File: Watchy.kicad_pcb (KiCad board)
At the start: 2 copper layers, 33.8 x 46 mm, 70 parts, among them J1 FPC24(0.5MM), J2 Micro USB, J3 Battery, M1 Vibration_Motor, Q1 AO3400A, Q2 UMH3N, Q4 CJ2301, Q5 S8050, SW1 BTN, SW2 BTN, SW3 BTN, SW4 BTN, U1 ESP32-PICO-D4, U2 ME6211C33M5G-N, U3 CP2102, U4 BMA423, U5 TP4054, U6 PCF8563BS, Y1 32.768KHz

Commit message: update to kicad 7
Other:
- net class Default removed

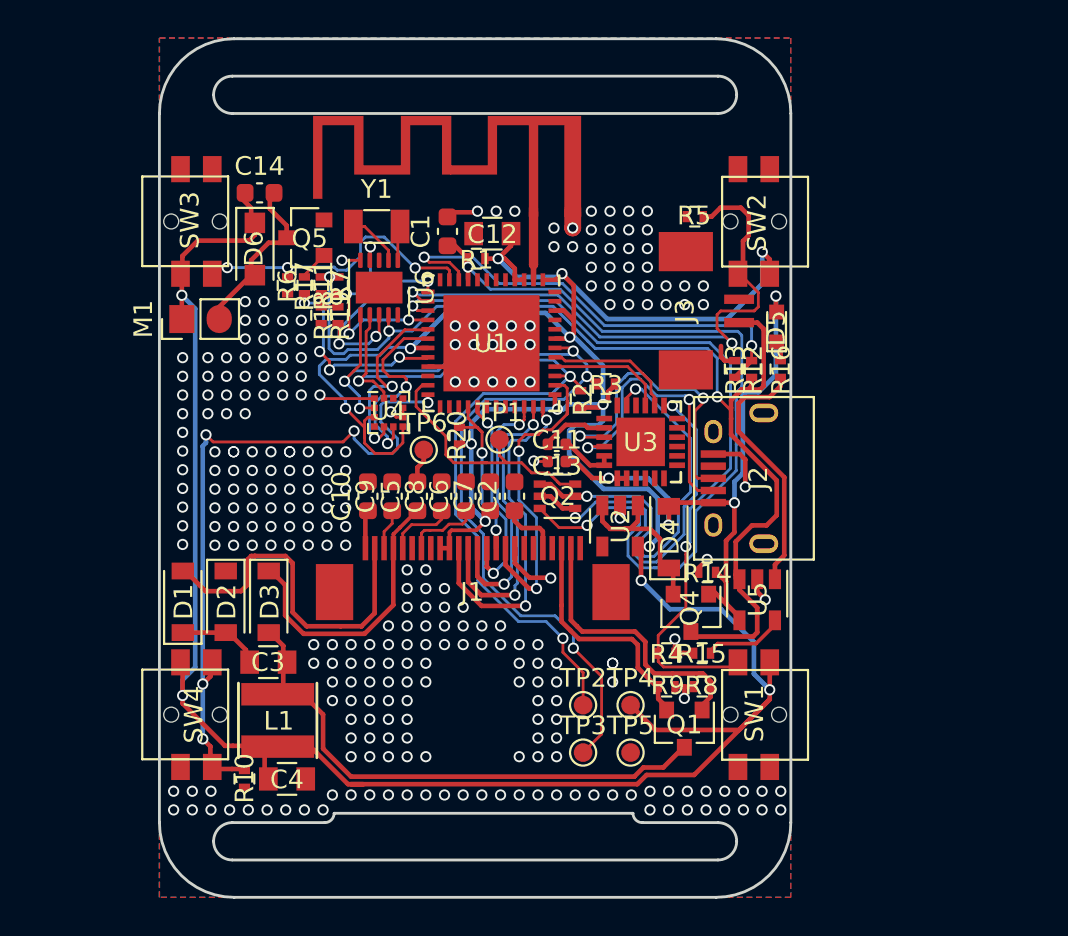
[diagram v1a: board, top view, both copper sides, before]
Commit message: add vib_mot footprint, remove all traces, rough positions
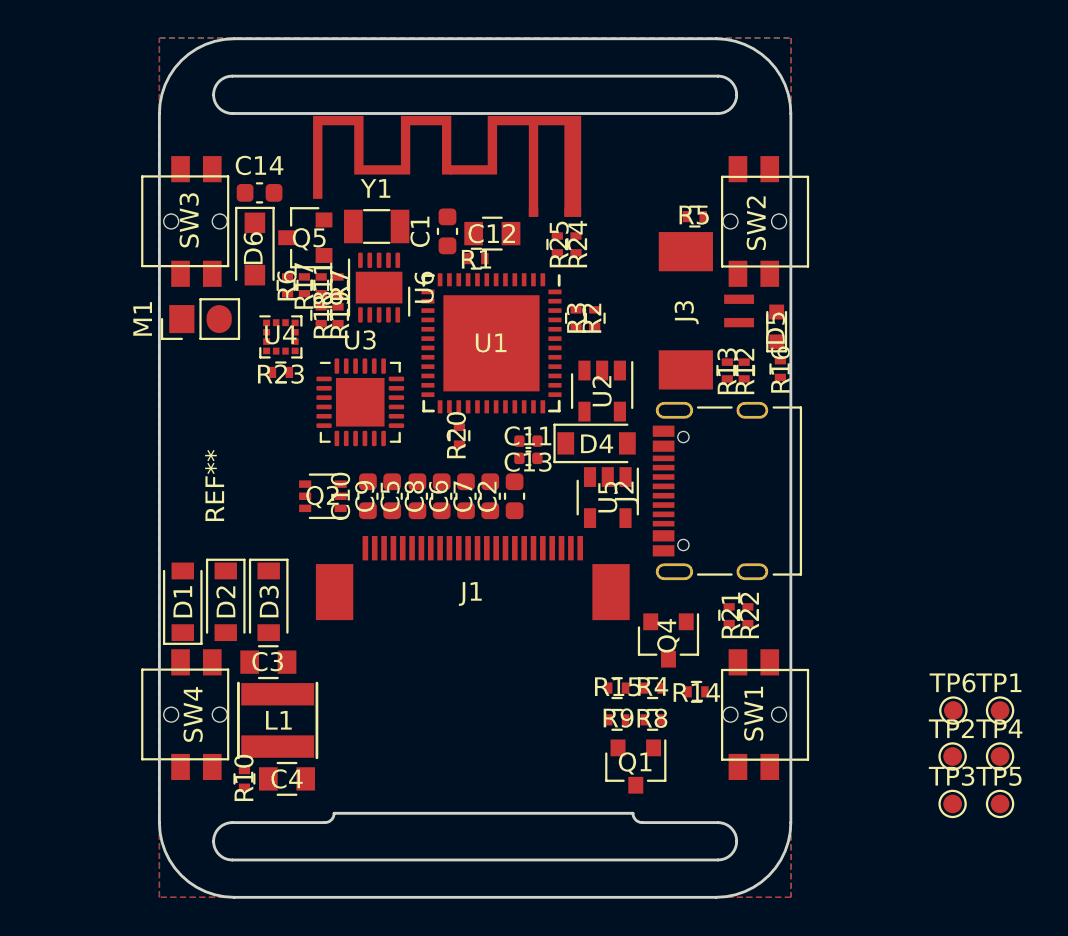
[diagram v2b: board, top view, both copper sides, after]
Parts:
- removed G***: LOGO, Watchy:sqfmi_duck
- removed G***: LOGO, Watchy:sqfmi_logo
- removed the REF** at (85.6, 93.2)
- added R21: 5.1k, Watchy:R_0402, F.Cu at (99.2, 101.0)
- added R22: 5.1k, Watchy:R_0402, F.Cu at (100.2, 101.0)
- added R23: 10K, Watchy:R_0402, F.Cu at (75.2, 88.0)
- added R24: 15k, Watchy:R_0402, F.Cu at (91.0, 81.2)
- added R25: 22k, Watchy:R_0402, F.Cu at (90.0, 81.2)
- added REF**: VIB_MOT_LBM0625A3098, Watchy:VIB_MOT_LBM0625A3098, F.Cu at (72.2, 94.1)
- J2: value Micro USB -> USB_C_Receptacle_USB2.0; footprint Watchy:USB_Micro-B -> Connector_USB:USB_C_Receptacle_Palconn_UTC16-G
- U3: footprint Housings_DFN_QFN:QFN-24-1EP_4x4mm_Pitch0.5mm -> Package_DFN_QFN:QFN-24-1EP_4x4mm_P0.5mm_EP2.6x2.6mm
- moved TP6 31.6 mm to (111.2, 106.1)
- moved TP1 30.5 mm to (113.7, 106.1)
- moved TP2 20.0 mm to (111.2, 108.6)
- moved TP3 20.0 mm to (111.2, 111.1)
- moved TP4 20.0 mm to (113.7, 108.6)
- moved TP5 20.0 mm to (113.7, 111.1)
- moved U3 15.2 mm to (79.5, 89.6)
- moved Q2 12.6 mm to (77.5, 94.6)
- moved U5 9.69 mm to (92.7, 94.7)
- moved U2 7.28 mm to (92.4, 89.0)
- moved U4 7.05 mm to (75.2, 86.1)
- moved R14 6.43 mm to (97.5, 105.1)
- moved D4 6.34 mm to (92.1, 91.8), turned to 0 degrees
- moved R15 4.92 mm to (93.2, 104.9), turned to 180 degrees
- moved R2 4.39 mm to (92.0, 85.1), turned to -90 degrees
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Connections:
- J1 pad 1: Net-(J1-Pad1) -> unconnected-(J1-Pin_1-Pad1)
- J1 pad 19: Net-(J1-Pad19) -> unconnected-(J1-Pin_19-Pad19)
- J1 pad 4: Net-(J1-Pad4) -> unconnected-(J1-Pin_4-Pad4)
- J1 pad 6: Net-(J1-Pad6) -> unconnected-(J1-Pin_6-Pad6)
- J1 pad 7: Net-(J1-Pad7) -> unconnected-(J1-Pin_7-Pad7)
- R16 pad 2: Net-(R16-Pad2) -> BATT_STAT
- U1 pad 12: Net-(U1-Pad12) -> BATT_STAT
- U1 pad 22: Net-(U1-Pad22) -> unconnected-(U1-IO2-Pad22)
- U1 pad 25: Net-(U1-Pad25) -> unconnected-(U1-IO16-Pad25)
- U1 pad 26: Net-(U1-Pad26) -> unconnected-(U1-VDD_SDIO-Pad26)
- U1 pad 27: Net-(U1-Pad27) -> unconnected-(U1-IO17-Pad27)
- U1 pad 30: Net-(U1-Pad30) -> unconnected-(U1-CMD-Pad30)
- U1 pad 31: Net-(U1-Pad31) -> unconnected-(U1-CLK-Pad31)
- U1 pad 32: Net-(U1-Pad32) -> unconnected-(U1-SD0-Pad32)
- U1 pad 33: Net-(U1-Pad33) -> unconnected-(U1-SD1-Pad33)
- U1 pad 44: Net-(U1-Pad44) -> unconnected-(U1-XTAL_N_NC-Pad44)
- U1 pad 45: Net-(U1-Pad45) -> unconnected-(U1-XTAL_P_NC-Pad45)
- U1 pad 47: Net-(U1-Pad47) -> unconnected-(U1-CAP2_NC-Pad47)
- U1 pad 48: Net-(U1-Pad48) -> unconnected-(U1-CAP1_NC-Pad48)
- U1 pad 5: Net-(U1-Pad5) -> unconnected-(U1-SENSOR_VP-Pad5)
- U1 pad 6: Net-(U1-Pad6) -> unconnected-(U1-SENSOR_CAPP-Pad6)
- U1 pad 7: Net-(U1-Pad7) -> unconnected-(U1-SENSOR_CAPN-Pad7)
- U2 pad 4: Net-(U2-Pad4) -> unconnected-(U2-NC-Pad4)
- U3 pad 1: Net-(U3-Pad1) -> unconnected-(U3-RI-Pad1)
- U3 pad 10: Net-(U3-Pad10) -> unconnected-(U3-VIO/NC-Pad10)
- U3 pad 11: Net-(U3-Pad11) -> unconnected-(U3-GPIO.3-Pad11)
- U3 pad 12: Net-(U3-Pad12) -> unconnected-(U3-GPIO.2-Pad12)
- U3 pad 13: Net-(U3-Pad13) -> unconnected-(U3-GPIO.1-Pad13)
- U3 pad 14: Net-(U3-Pad14) -> unconnected-(U3-GPIO.0-Pad14)
- U3 pad 15: Net-(U3-Pad15) -> unconnected-(U3-~{SUSPEND}-Pad15)
- U3 pad 16: Net-(U3-Pad16) -> unconnected-(U3-VPP-Pad16)
- U3 pad 17: Net-(U3-Pad17) -> unconnected-(U3-SUSPEND-Pad17)
- U3 pad 18: Net-(U3-Pad18) -> unconnected-(U3-CTS-Pad18)
- U3 pad 22: Net-(U3-Pad22) -> unconnected-(U3-DSR-Pad22)
- U3 pad 24: Net-(U3-Pad24) -> unconnected-(U3-DCD-Pad24)
- U3 pad 25: Net-(U3-Pad25) -> unconnected-(U3-PAD-Pad25)
- U3 pad 3: Net-(J2-Pad3) -> Net-(U3-D+)
- U3 pad 4: Net-(J2-Pad2) -> Net-(U3-D-)
- U3 pad 9: Net-(U3-Pad9) -> unconnected-(U3-~{RST}-Pad9)
- U4 pad 10: Net-(U4-Pad10) -> +3V3
- U4 pad 11: Net-(U4-Pad11) -> unconnected-(U4-ASCL-Pad11)
- U4 pad 4: Net-(U4-Pad4) -> unconnected-(U4-ASDA-Pad4)
- U5 pad 1: Net-(R16-Pad2) -> BATT_STAT
- U6 pad 10: Net-(U6-Pad10) -> unconnected-(U6-NC-Pad10)
- U6 pad 3: Net-(U6-Pad3) -> unconnected-(U6-NC-Pad3)
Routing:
- net +3V3: track 191.4 -> 0.00 mm, vias 15 -> 0
- net +BATT: track 59.5 -> 0.00 mm, vias 3 -> 0
- net SDA: track 52.9 -> 0.00 mm, vias 5 -> 0
- net EN: track 45.9 -> 0.00 mm, vias 2 -> 0
- net SCL: track 45.7 -> 0.00 mm, vias 3 -> 0
- net BTN_1: track 41.5 -> 0.00 mm, vias 2 -> 0
- net BTN_4: track 38.1 -> 0.00 mm, vias 5 -> 0
- net VBUS: track 35.2 -> 0.00 mm, vias 4 -> 0
- net BTN_2: track 31.2 -> 0.00 mm, vias 2 -> 0
- net GND: track 30.5 -> 0.00 mm, vias 275 -> 0
- net Net-(D3-A): track 30.2 -> 0.00 mm
- net ADC: track 24.6 -> 0.00 mm, vias 2 -> 0
- net DTR: track 21.9 -> 0.00 mm, vias 2 -> 0
- net RTS: track 21.0 -> 0.00 mm, vias 2 -> 0
- net PREVGL: track 19.5 -> 0.00 mm
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
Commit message: erstes Layout, buttons fehlen
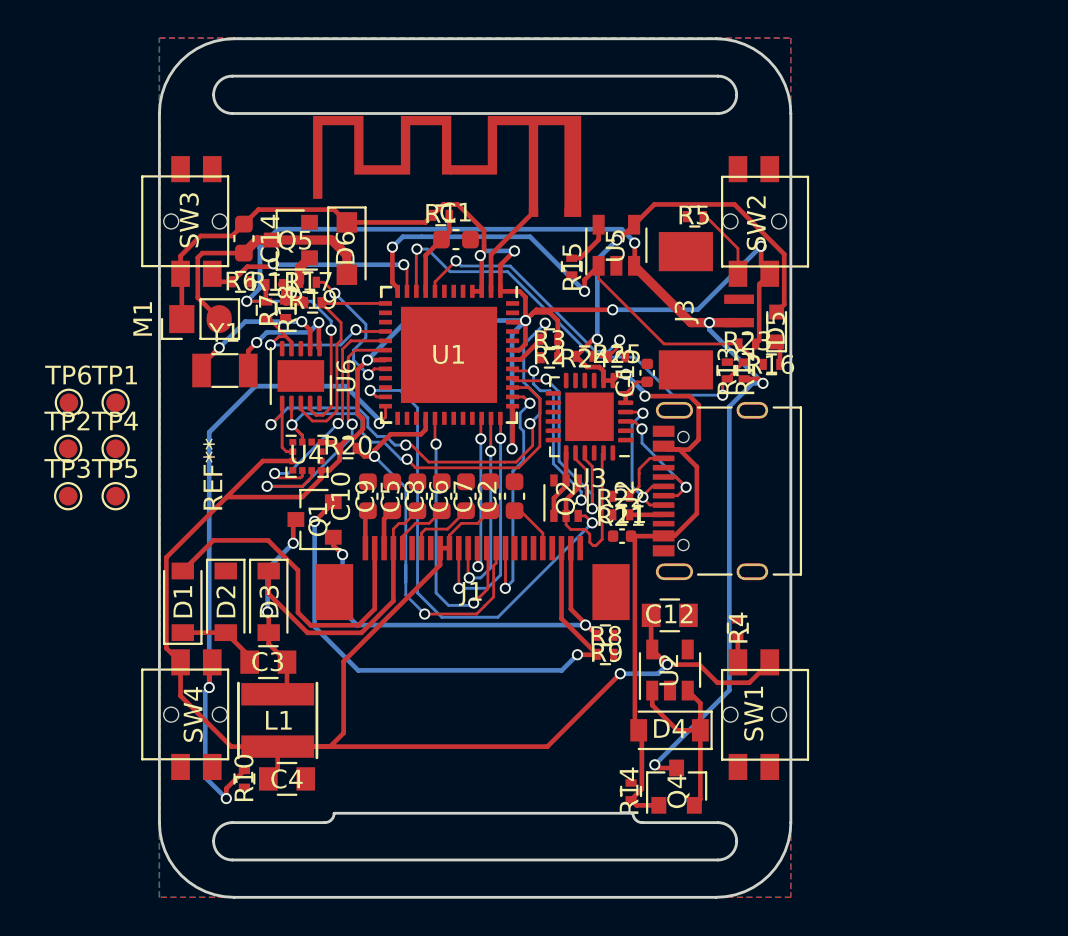
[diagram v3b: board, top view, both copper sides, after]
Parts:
- AE1: value SWRA117D -> Val**
- moved TP1 50.1 mm to (66.4, 89.6)
- moved TP4 50.1 mm to (66.4, 92.1)
- moved TP5 50.1 mm to (66.4, 94.6)
- moved TP6 50.1 mm to (63.9, 89.6)
- moved TP2 50.1 mm to (63.8, 92.1)
- moved TP3 50.1 mm to (63.8, 94.6)
- moved R23 25.0 mm to (100.2, 86.5), turned to 0 degrees
- moved R15 22.7 mm to (90.8, 82.3), turned to 90 degrees
- moved C12 22.5 mm to (96.0, 101.0), turned to 0 degrees
- moved Q1 21.7 mm to (77.0, 95.9), turned to 180 degrees
- moved D4 15.8 mm to (96.0, 107.2), turned to 180 degrees
- moved U2 15.4 mm to (96.0, 103.9), turned to 90 degrees
- moved U5 13.5 mm to (93.2, 81.2), turned to 90 degrees
- moved Q2 13.0 mm to (90.5, 94.7), turned to 90 degrees
- moved U3 12.3 mm to (91.7, 90.4), turned to 180 degrees
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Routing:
- net +3V3: track 0.00 -> 171.4 mm, vias 0 -> 9
- net +BATT: track 0.00 -> 75.4 mm, vias 0 -> 6
- net VBUS: track 0.00 -> 58.4 mm, vias 0 -> 4
- net BTN_4: track 0.00 -> 35.6 mm, vias 0 -> 3
- net SDA: track 0.00 -> 31.2 mm, vias 0 -> 4
- net RESE: track 0.00 -> 30.0 mm, vias 0 -> 2
- net BATT_STAT: track 0.00 -> 27.3 mm, vias 0 -> 2
- net GPIO0: track 0.00 -> 26.7 mm, vias 0 -> 2
- net ADC: track 0.00 -> 24.1 mm, vias 0 -> 2
- net SCL: track 0.00 -> 23.3 mm, vias 0 -> 2
- net GDR: track 0.00 -> 22.7 mm, vias 0 -> 2
- net RES: track 0.00 -> 22.5 mm, vias 0 -> 2
- net PREVGL: track 0.00 -> 17.8 mm
- net ACC_INT_2: track 0.00 -> 15.2 mm, vias 0 -> 2
- net Net-(U1-SENSOR_VN): track 0.00 -> 15.1 mm, vias 0 -> 2
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
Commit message: Gerbers erstellt
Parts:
- removed TP1: GPIO0, TestPoint:TestPoint_Pad_D1.0mm
- removed TP2: SCL, TestPoint:TestPoint_Pad_D1.0mm
- removed TP3: SDA, TestPoint:TestPoint_Pad_D1.0mm
- removed TP4: 3V3, TestPoint:TestPoint_Pad_D1.0mm
- removed TP5, TP6: GND, TestPoint:TestPoint_Pad_D1.0mm
- AE1: value Val** -> SWRA117D
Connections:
- U3 pad 25: unconnected-(U3-PAD-Pad25) -> GND
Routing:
- net GND: track 0.00 -> 62.7 mm, vias 0 -> 170
- net BTN_1: track 1.38 -> 57.9 mm, vias 0 -> 4
- net EN: track 4.59 -> 43.4 mm, vias 0 -> 4
- net unconnected-(J2-SHIELD-PadS1): track 0.00 -> 23.6 mm
- net BTN_2: track 3.92 -> 27.2 mm, vias 0 -> 4
- net SCL: track 23.3 -> 29.5 mm, vias 2 -> 4
- net ADC: track 24.1 -> 27.6 mm
- net DTR: track 10.1 -> 8.73 mm
- net Net-(U1-SENSOR_VN): track 15.1 -> 16.4 mm
- net TX: track 12.3 -> 11.5 mm
- net Net-(U3-D-): track 8.62 -> 9.38 mm
- net RX: track 13.0 -> 13.7 mm

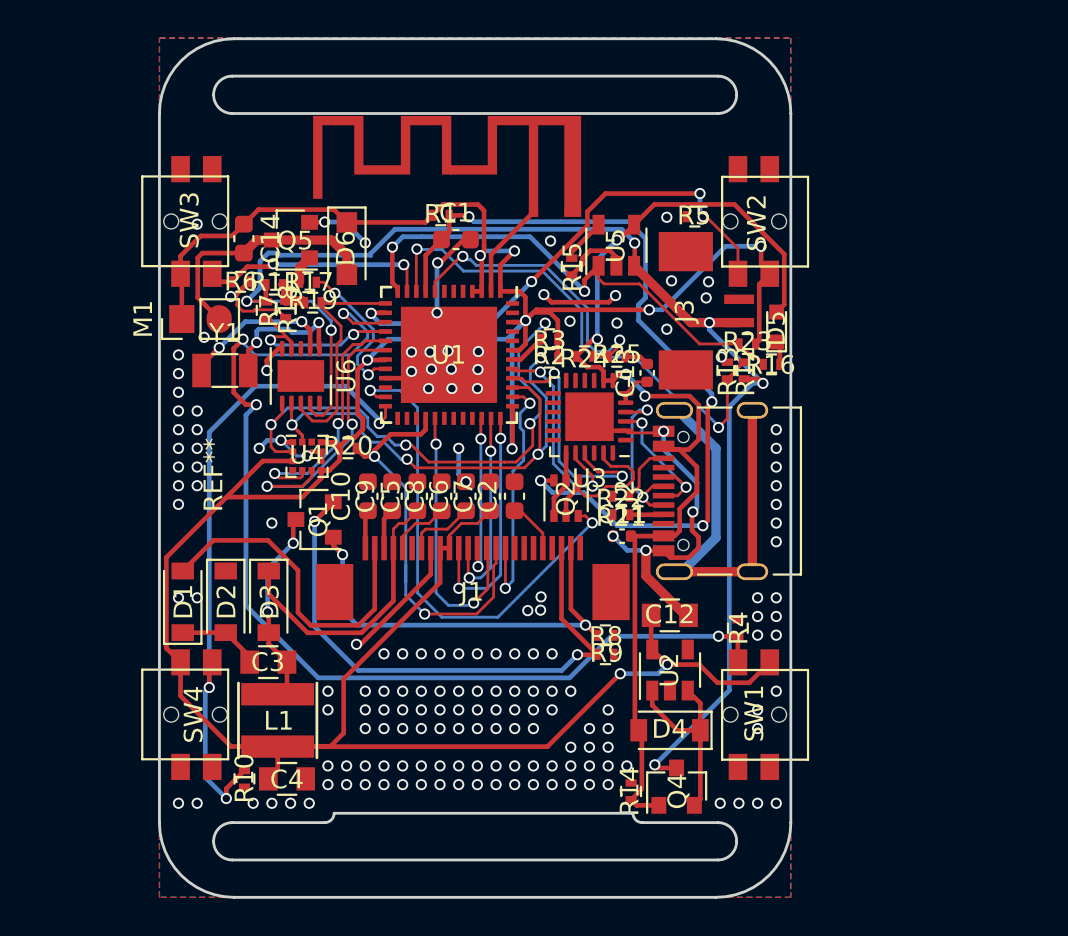
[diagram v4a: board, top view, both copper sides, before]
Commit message: fix: unconnected GNDs
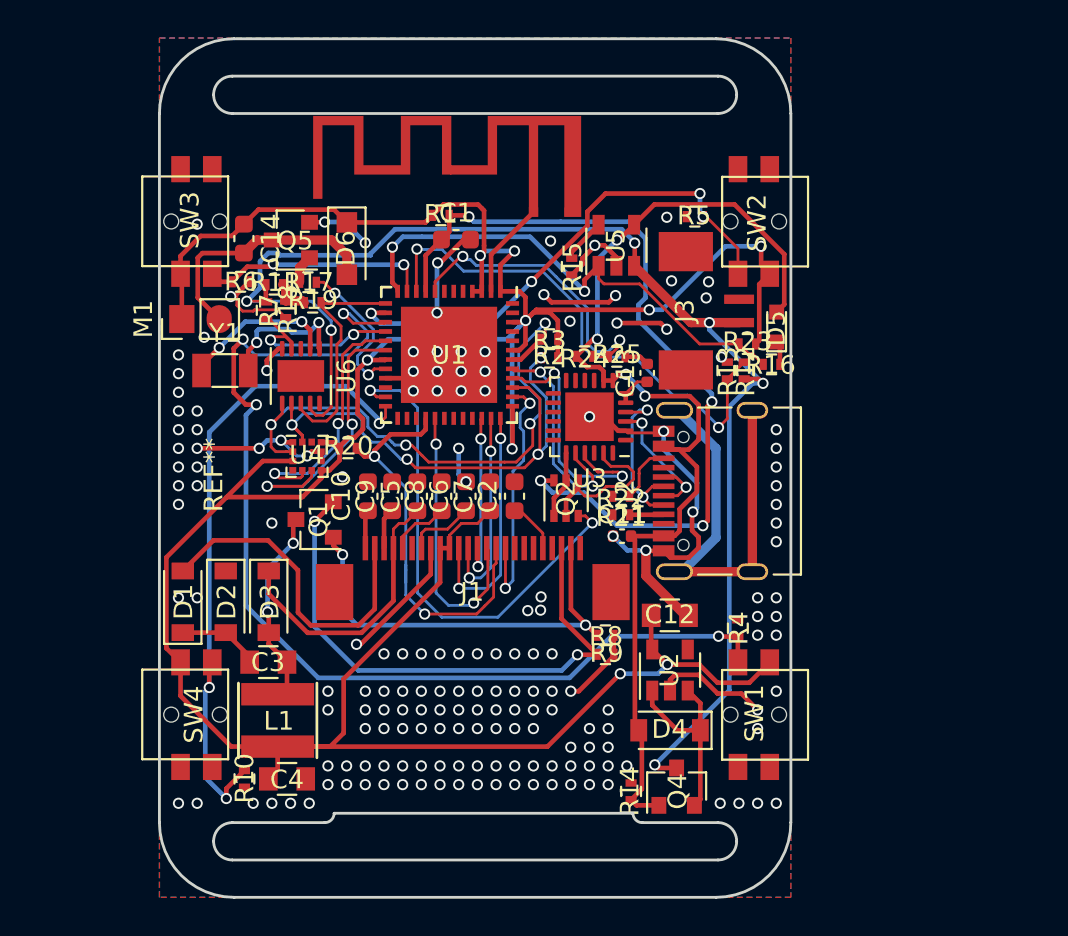
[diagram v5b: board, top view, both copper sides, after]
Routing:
- net GND: track 62.7 -> 79.6 mm, vias 170 -> 174

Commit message: fix: inconsistent and missing footprints
May have broken something.
Also updated the PCB with the new footprints.
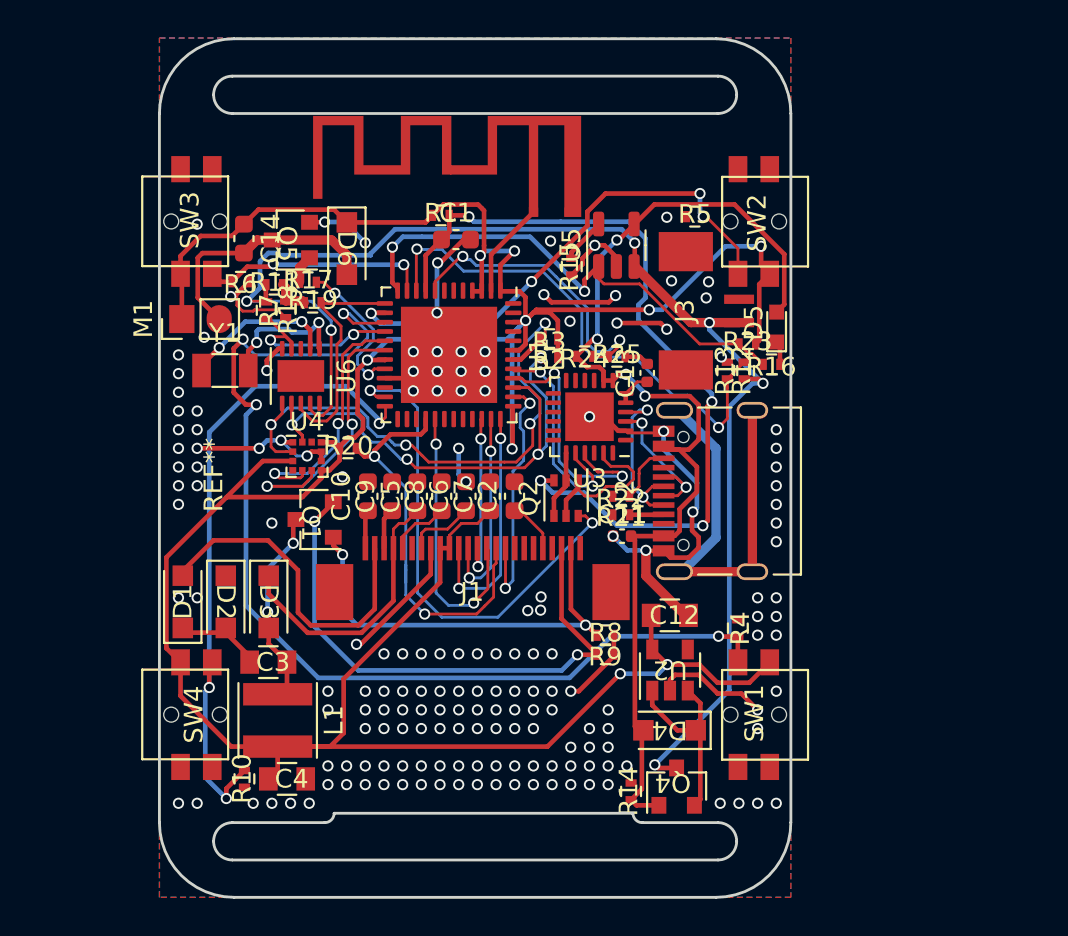
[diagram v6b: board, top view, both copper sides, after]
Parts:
- C12, C3, C4: footprint Capacitors_SMD:C_0805 -> Watchy:C_0805
- D1, D2, D3, D4: footprint Diodes_SMD:D_SOD-123 -> Watchy:D_SOD-123
- D5: footprint LEDs:LED_0603 -> Watchy:LED_0603
- D6: footprint Diodes_SMD:D_SOD-123F -> Watchy:D_SOD-123
- L1: footprint Inductors:Inductor_Taiyo-Yuden_NR-40xx -> Inductor_SMD:L_Taiyo-Yuden_NR-40xx
- Q1, Q4, Q5: footprint TO_SOT_Packages_SMD:SOT-23 -> Watchy:SOT-23
- Q2: footprint TO_SOT_Packages_SMD:SOT-363_SC-70-6 -> Package_TO_SOT_SMD:SOT-363_SC-70-6
- R1, R10, R12, R13, R14, R15, R16, R17, R2, R3, R4, R5, R6, R7, R8, R9: footprint Resistors_SMD:R_0402 -> Watchy:R_0402
- U1: footprint Housings_DFN_QFN:QFN-48-1EP_7x7mm_Pitch0.5mm -> Package_DFN_QFN:QFN-48-1EP_7x7mm_P0.5mm_EP5.15x5.15mm
- U2: footprint TO_SOT_Packages_SMD:SOT-23-5 -> Watchy:SOT-23-5
- U4: footprint Housings_LGA:LGA-12_2x2mm_Pitch0.5mm -> Package_LGA:LGA-12_2x2mm_P0.5mm
- U5: footprint TO_SOT_Packages_SMD:SOT-23-5 -> Package_TO_SOT_SMD:SOT-23-5

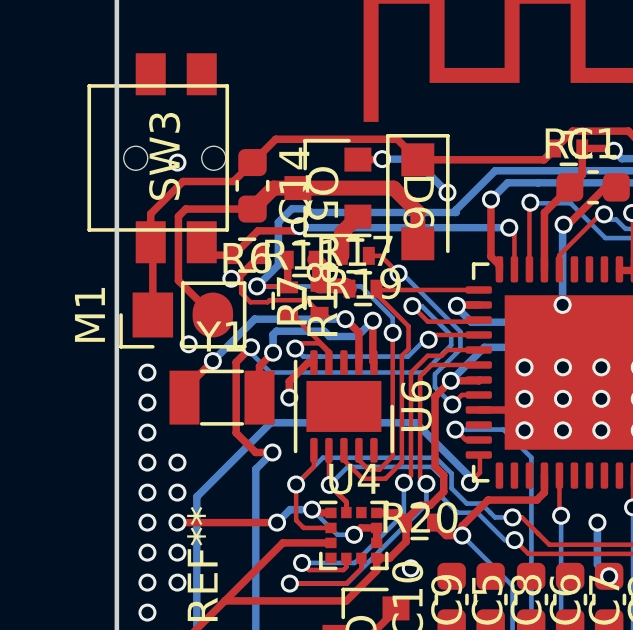
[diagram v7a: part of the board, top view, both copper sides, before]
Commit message: actually update all footprint
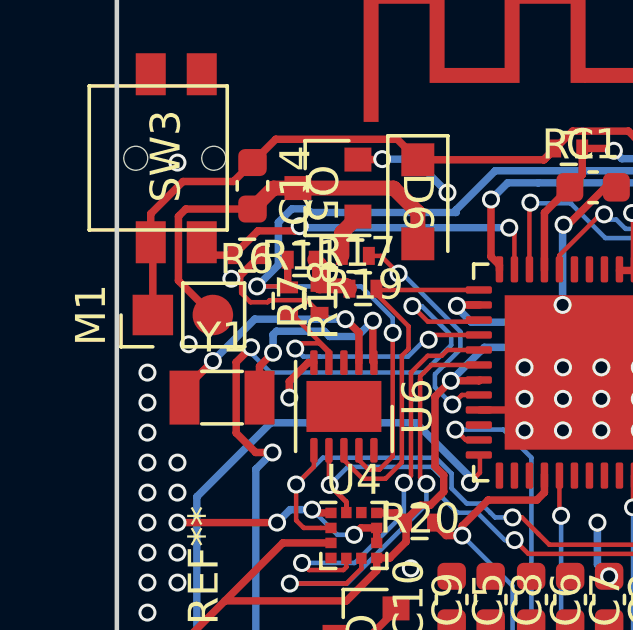
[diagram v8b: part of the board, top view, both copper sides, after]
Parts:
- AE1: value SWRA117D -> Val**
